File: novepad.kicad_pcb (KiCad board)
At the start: 4 copper layers, 99.5 x 58 mm, 150 parts, among them J101 NOVENA_LCD_CONN, J102 LP097QX1_CONN, J401 MOLEX_502250-8037, J402 MOLEX_502250-8037, U201 TPS61181, U202 TPS61181, U301 IT6251, U401 FT5816LPC, X301 27MHz 50ppm, 8-18pF, ESR < 80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, X401 12MHz 18pF

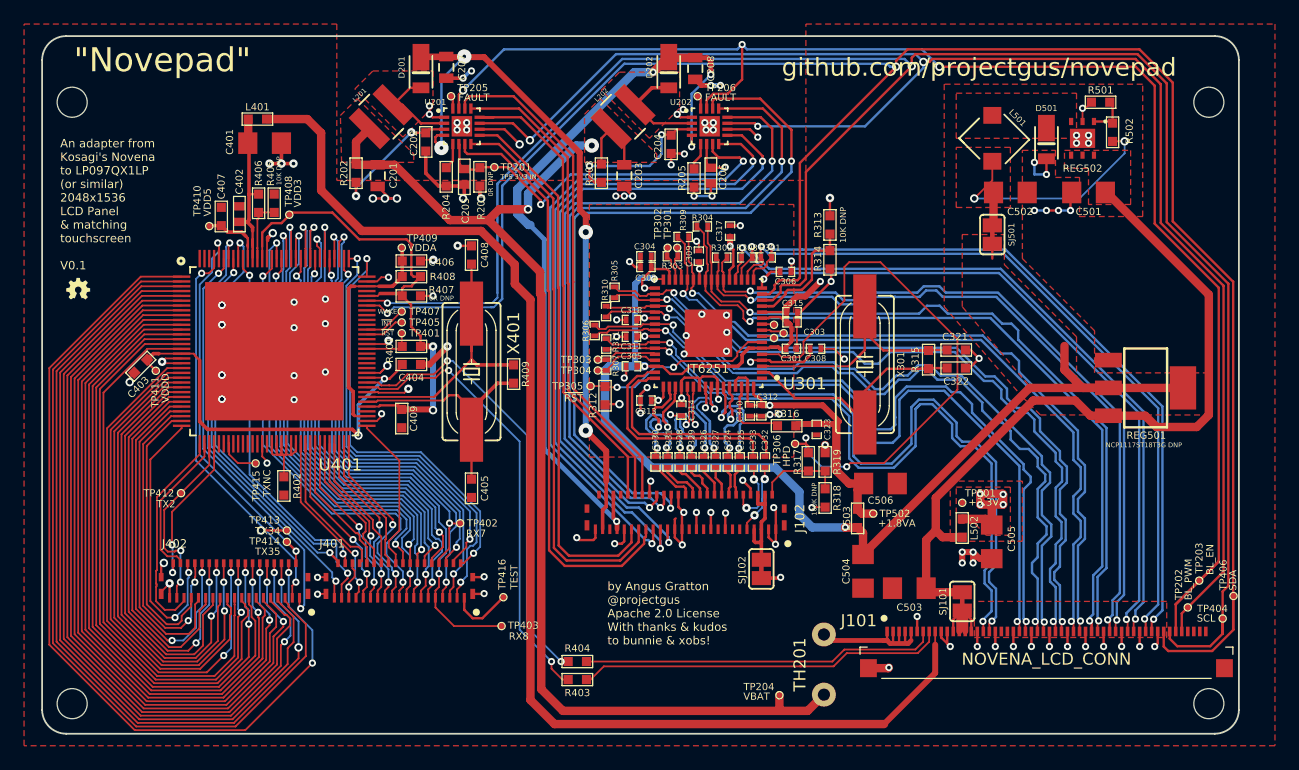
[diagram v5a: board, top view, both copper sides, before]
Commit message: Add 4 additional 3.3V decoupling capacitors for the 3.3V power plane
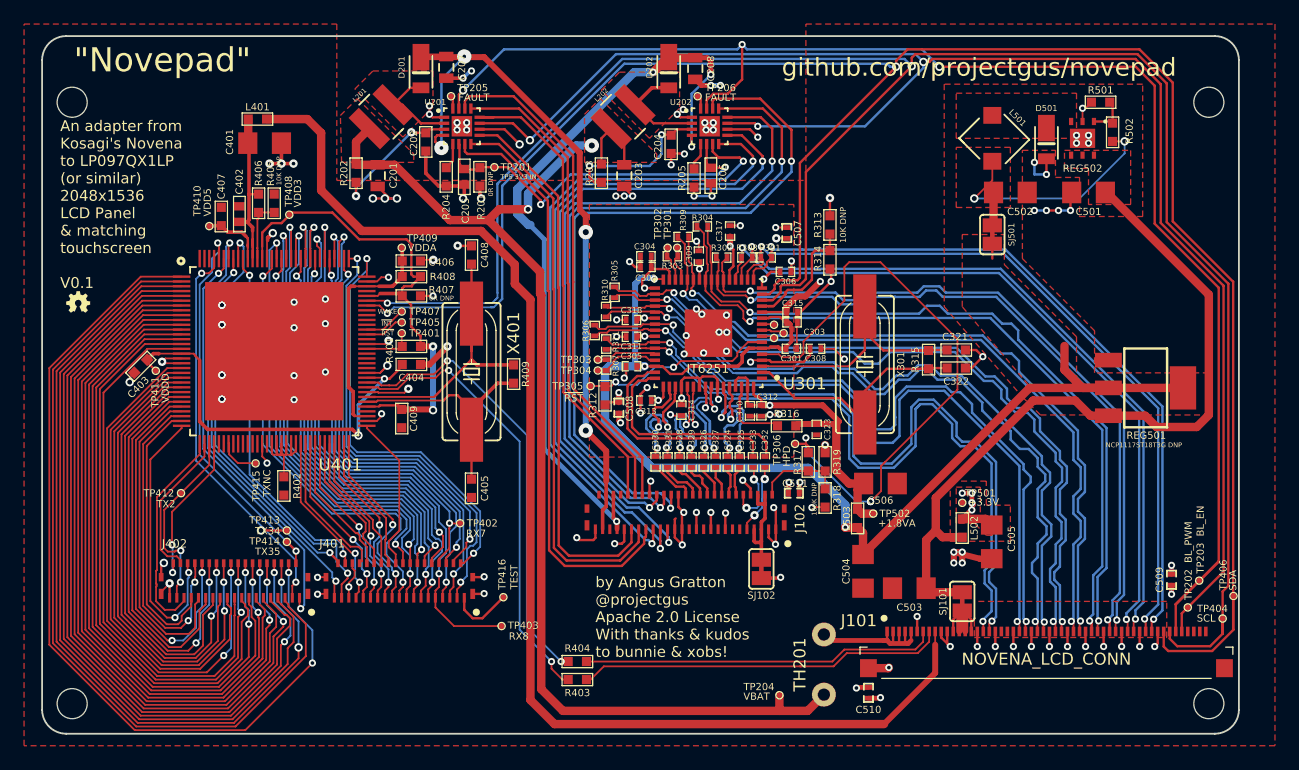
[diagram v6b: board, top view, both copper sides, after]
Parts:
- added C507: 1uF 25V X5R, SMD_Packages:SMD-0402_c, F.Cu at (147.4, 113.4)
- added C508: 100nF 25V X5R, SMD_Packages:SMD-0402_c, F.Cu at (133.4, 127.9)
- added C509: 100nF 25V X5R, SMD_Packages:SMD-0402_c, F.Cu at (179.4, 142.2)
- added C510: 100nF 25V X5R, SMD_Packages:SMD-0402_c, F.Cu at (154.2, 151.6)
- added C511: 100nF 25V X5R, SMD_Packages:SMD-0402_c, F.Cu at (148.0, 135.0)
- moved LOGO_OSHW_silkscreen_2mm 1.10 mm to (88.5, 119.1)
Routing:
- net +1.8V: track 114.9 -> 120.4 mm
- net GND: track 258.2 -> 262.3 mm, vias 128 -> 136
- net /LVDS to eDP Conversion/HPD: track 47.8 -> 51.5 mm, vias 2 -> 3
- net Net-(R312-Pad2): track 17.1 -> 17.9 mm
- net +3.3V: track 30.4 -> 31.0 mm, vias 13 -> 17

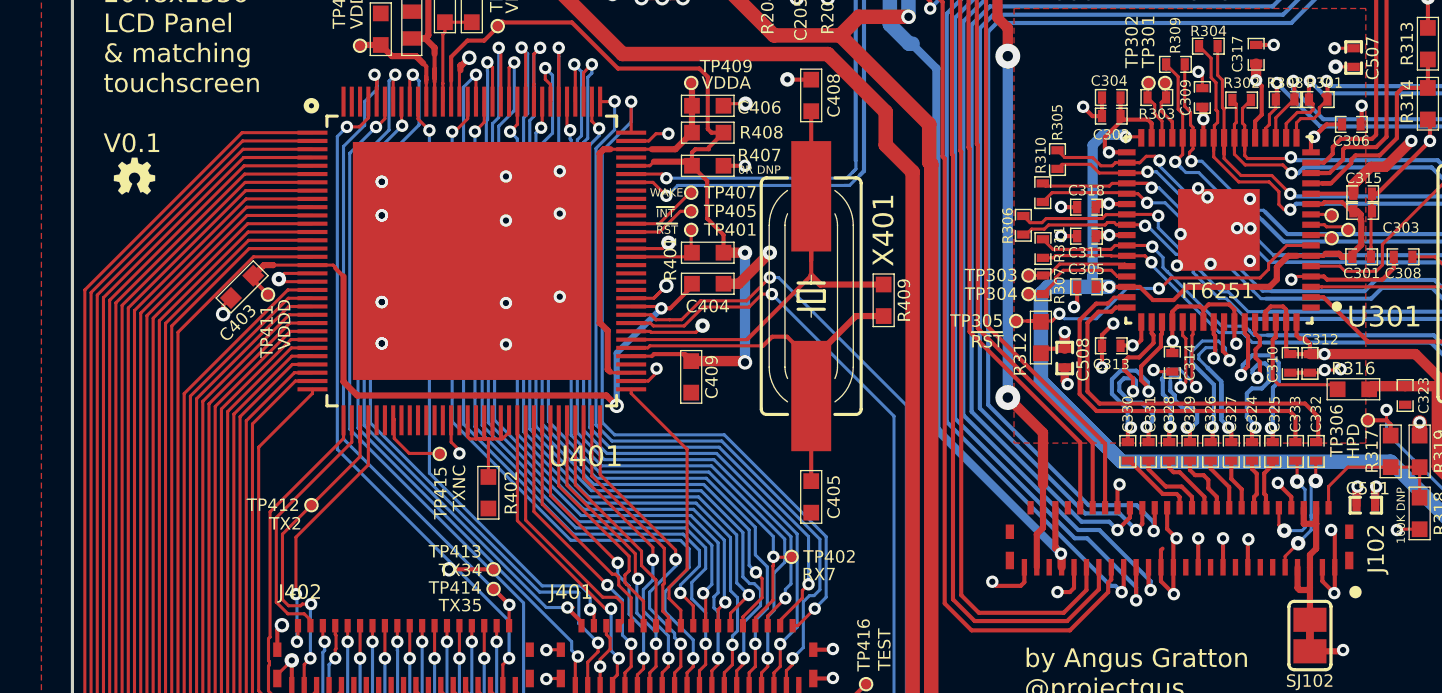
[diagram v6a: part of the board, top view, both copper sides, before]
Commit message: Reroute tight loop for V0.2, redo length matching with tighter constraints (not for any particular reason)
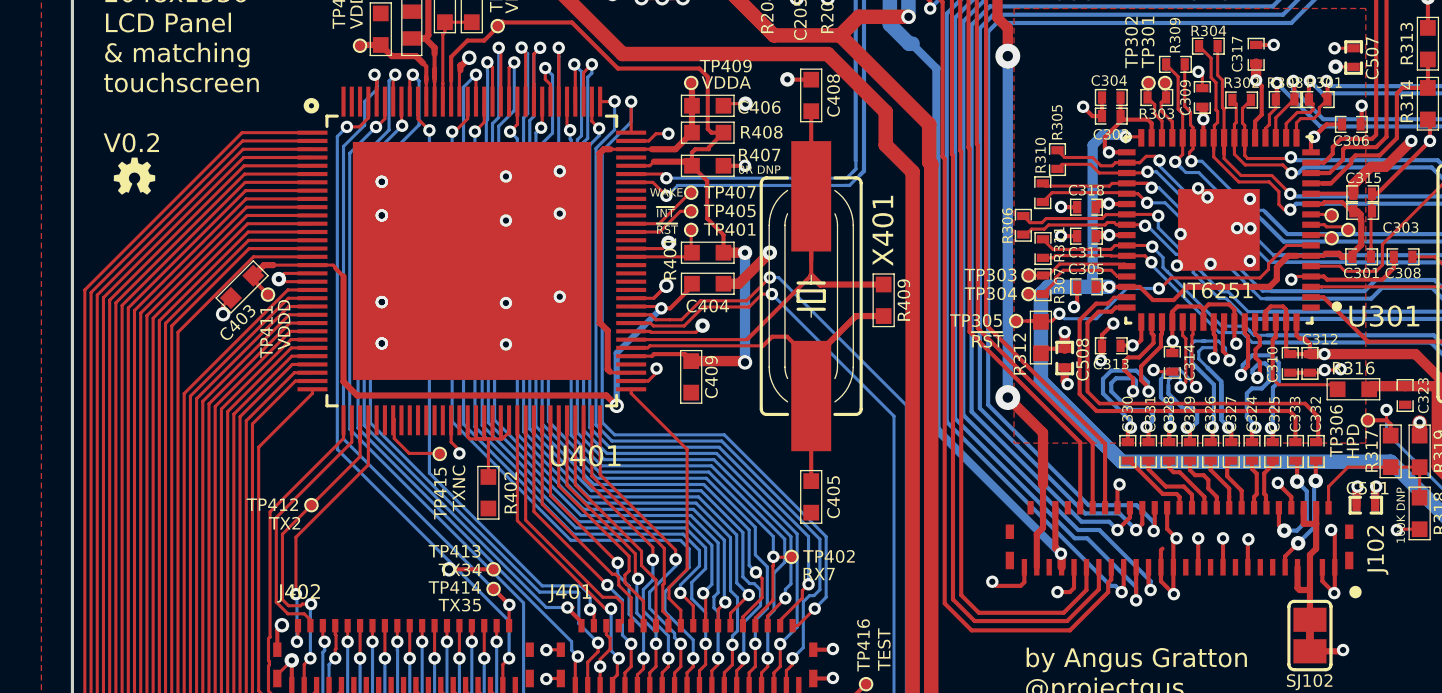
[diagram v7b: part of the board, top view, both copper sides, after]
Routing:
- net /LVDS to eDP Conversion/L3_N: track 9.96 -> 10.8 mm
- net /LVDS to eDP Conversion/L3_P: track 10.0 -> 10.6 mm
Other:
- net class eDP_ACC_DP0.15/5 added: clearance 0.15, trace_width 0.175, via_dia 0.6, via_drill 0.3
- net class eDP_ACC_DP0.2/5 removed
- net class eDP_AUX_DP0.15/5 added: clearance 0.15, trace_width 0.175, via_dia 0.6, via_drill 0.3
- net class eDP_AUX_DP0.2/5 removed
- net class eDP_AUX_OUT_DP0.15/5 added: clearance 0.15, trace_width 0.175, via_dia 0.6, via_drill 0.3
- net class eDP_AUX_OUT_DP0.2/5 removed
- net class eDP_DP0.15/5 added: clearance 0.15, trace_width 0.175, via_dia 0.6, via_drill 0.3
- net class eDP_DP0.2/5 removed
- board text added: "An adapter from Kosagi's Novena to LP097QX1LP (or similar) 2048x1536 LCD Panel & matching touchscreen V0.2"
- board text removed: "An adapter from Kosagi's Novena to LP097QX1LP (or similar) 2048x1536 LCD Panel & matching touchscreen V0.1"
